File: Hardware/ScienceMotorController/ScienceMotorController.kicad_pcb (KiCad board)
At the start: 2 copper layers, 125.7 x 166.4 mm, 148 parts, among them U1 VNH5019A_E, U10 PMN280ENEAX, U11 PMN280ENEAX, U12 LT1910, U13 LT1910, U14 LT1910, U15 5VA OKI, U2 VNH5019A_E, U3 VNH5019A_E, U4 VNH5019A_E, U5 5V OKI, U6 TM4C129E_Launchpad, U7 3V3 OKI, U8 5VA OKI, U9 PMN280ENEAX

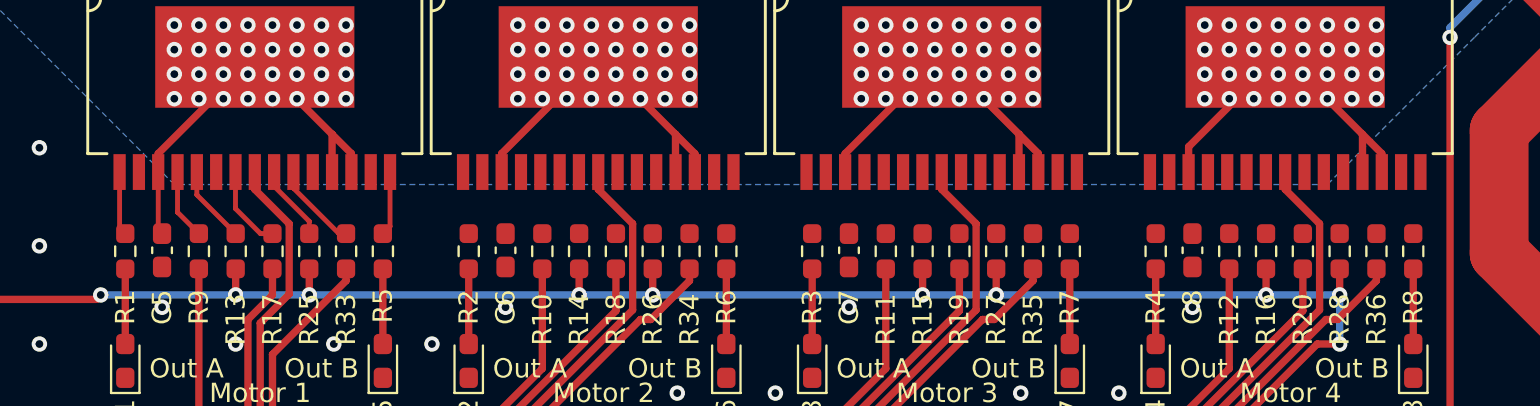
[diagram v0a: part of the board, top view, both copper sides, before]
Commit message: Traces Under Mocos
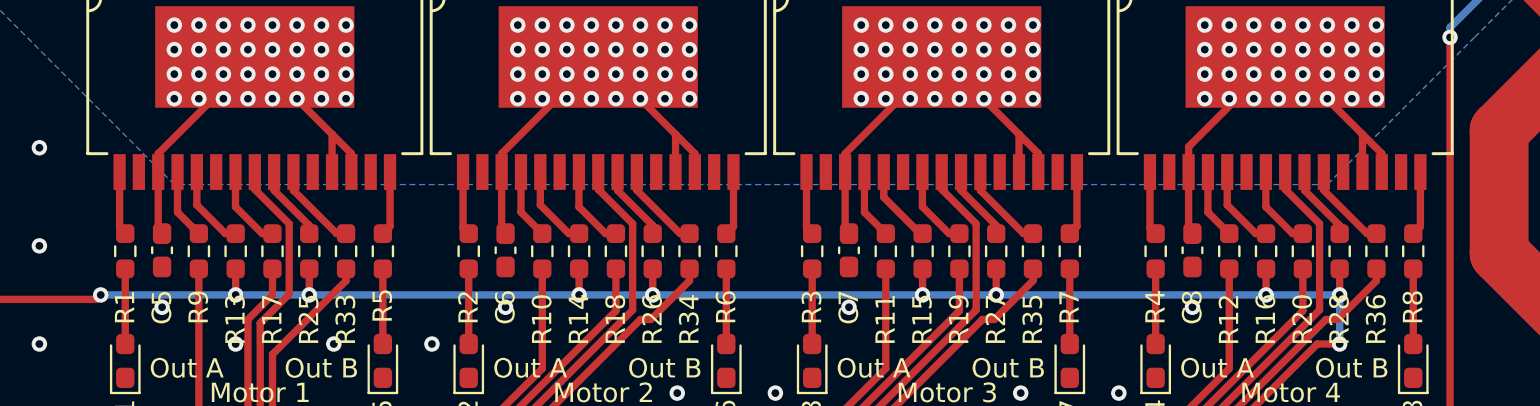
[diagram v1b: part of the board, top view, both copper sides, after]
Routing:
- net +12VA: track 263.1 -> 272.9 mm
- net Net-(R36-Pad1): track 0.00 -> 4.60 mm
- net Net-(R35-Pad1): track 0.00 -> 4.60 mm
- net Net-(R34-Pad1): track 0.00 -> 4.60 mm
- net Net-(R14-Pad1): track 0.00 -> 4.33 mm
- net Net-(R16-Pad1): track 0.00 -> 4.33 mm
- net Net-(R18-Pad1): track 0.00 -> 4.29 mm
- net Net-(R20-Pad1): track 0.00 -> 4.29 mm
- net Net-(R19-Pad1): track 0.00 -> 4.29 mm
- net Net-(R15-Pad1): track 0.00 -> 4.10 mm
- net Net-(R28-Pad1): track 0.00 -> 3.94 mm
- net Net-(R27-Pad1): track 0.00 -> 3.94 mm
- net Net-(R26-Pad1): track 0.00 -> 3.94 mm
- net Net-(R12-Pad1): track 0.00 -> 3.65 mm
- net Net-(R11-Pad1): track 0.00 -> 3.65 mm
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
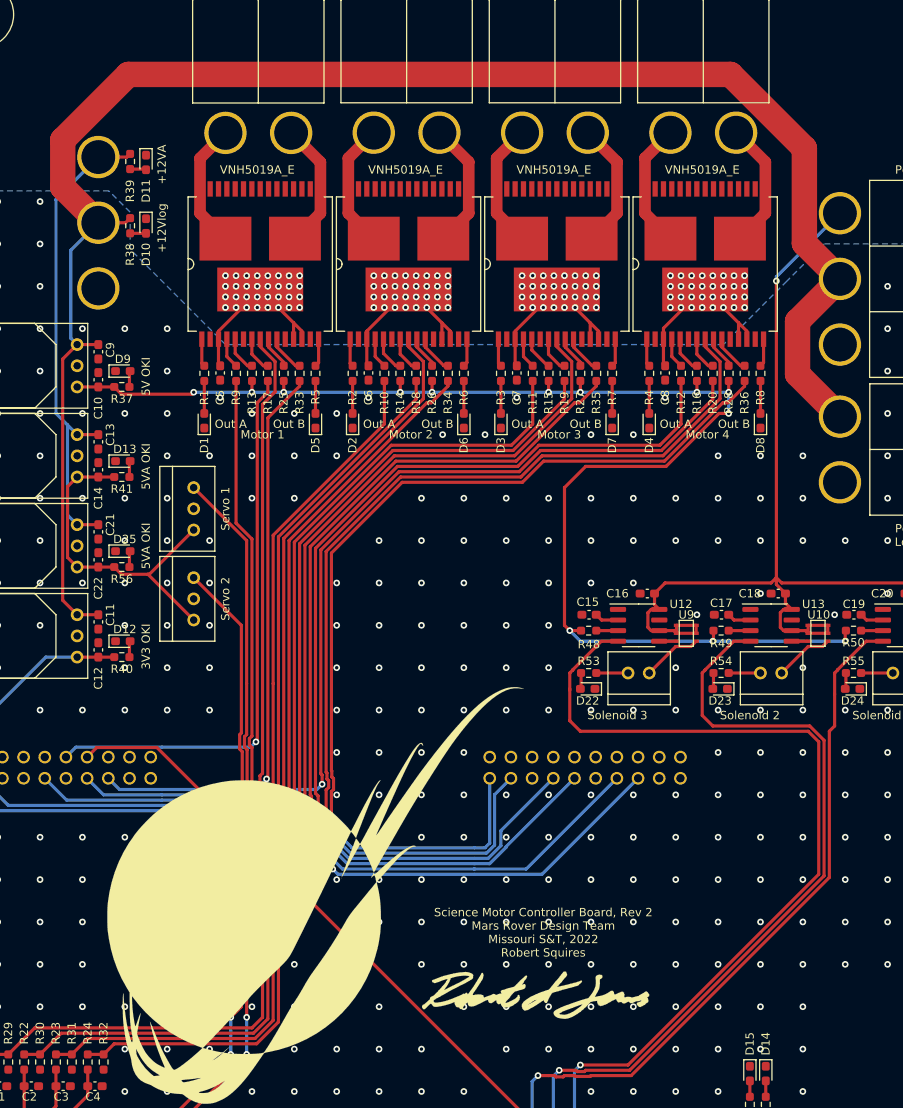
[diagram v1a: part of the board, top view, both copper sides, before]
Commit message: Changed Ground Plane for Motor Stalls
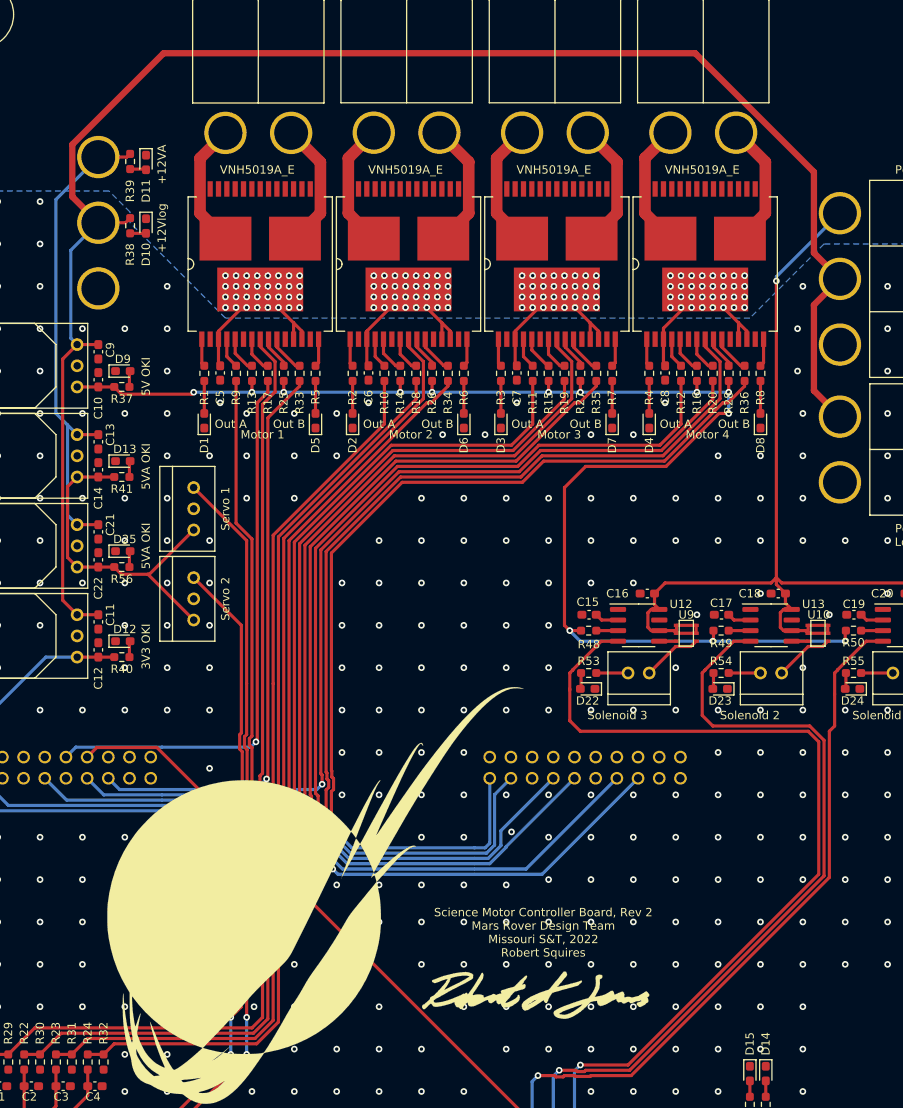
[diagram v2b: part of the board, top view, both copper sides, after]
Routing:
- net +12V: track 204.9 -> 202.4 mm
- net GND: vias 432 -> 438

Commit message: Board Review Changes
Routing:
- net GND: vias 438 -> 421
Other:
- outline, holes or cut-outs redrawn
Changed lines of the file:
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@@
   (general
     (thickness 1.6)
-    (drawings 47)
-    (tracks 1377)
+    (drawings 52)
+    (tracks 1361)
     (zones 0)
     (modules 148)
@@
     )
   )
+  (gr_line (start 141.605 101.6) (end 158.115 101.6) (layer Edge.Cuts) (width 0.05))
+  (gr_line (start 141.605 80.645) (end 141.605 101.6) (layer Edge.Cuts) (width 0.05))
+  (gr_line (start 158.115 80.645) (end 141.605 80.645) (layer Edge.Cuts) (width 0.05))
+  (gr_line (start 160.02 78.105) (end 160.02 78.74) (layer Edge.Cuts) (width 0.05))
+  (gr_arc (start 158.115 78.74) (end 158.115 80.645) (angle -90) (layer Edge.Cuts) (width 0.05))
+  (gr_arc (start 158.115 103.505) (end 160.02 103.505) (angle -90) (layer Edge.Cuts) (width 0.05))
+  (gr_arc (start 156.21 -35.56) (end 160.02 -35.56) (angle -90) (layer Edge.Cuts) (width 0.05))
+  (gr_line (start 160.02 78.105) (end 160.02 -35.56) (layer Edge.Cuts) (width 0.05))
+  (gr_line (start 160.02 123.19) (end 160.02 103.505) (layer Edge.Cuts) (width 0.05))
   (gr_text "Science Motor Controller Board, Rev 2\nMars Rover Design Team\nMissouri S&T, 2022\nRobert Squires" (at 106.045 74.93) (layer F.SilkS)
     (effects (font (size 1 1) (thickness 0.15)))
@@
   )
   (gr_line (start 156.21 127) (end 38.1 127) (layer Edge.Cuts) (width 0.05))
-  (gr_line (start 160.02 113.665) (end 160.02 123.19) (layer Edge.Cuts) (width 0.05))
-  (gr_line (start 160.02 -35.56) (end 160.02 -31.115) (layer Edge.Cuts) (width 0.05))
   (gr_line (start 38.1 -39.37) (end 156.21 -39.37) (layer Edge.Cuts) (width 0.05))
   (gr_line (start 34.29 -35.56) (end 34.29 -31.115) (layer Edge.Cuts) (width 0.05))
   (gr_arc (start 38.1 -35.56) (end 38.1 -39.37) (angle -90) (layer Edge.Cuts) (width 0.05))
-  (gr_arc (start 156.21 -35.56) (end 160.02 -35.56) (angle -90) (layer Edge.Cuts) (width 0.05))
   (gr_arc (start 156.21 123.19) (end 156.21 127) (angle -90) (layer Edge.Cuts) (width 0.05))
   (gr_arc (start 38.1 123.19) (end 34.29 123.19) (angle -90) (layer Edge.Cuts) (width 0.05))
   (gr_line (start 34.29 118.11) (end 34.29 123.19) (layer Edge.Cuts) (width 0.05))
-  (gr_line (start 160.02 -31.115) (end 160.02 113.665) (layer Edge.Cuts) (width 0.05))
   (gr_line (start 34.29 -31.115) (end 34.29 118.11) (layer Edge.Cuts) (width 0.05))
   (segment (start 55.054501 98.226501) (end 53.904 97.076) (width 0.381) (layer F.Cu) (net 1))
@@
   (via (at 147.32 -2.54) (size 0.8) (drill 0.4) (layers F.Cu B.Cu) (net 2))
   (via (at 152.4 -2.54) (size 0.8) (drill 0.4) (layers F.Cu B.Cu) (net 2))
-  (via (at 157.48 -2.54) (size 0.8) (drill 0.4) (layers F.Cu B.Cu) (net 2))
-  (via (at 157.48 2.54) (size 0.8) (drill 0.4) (layers F.Cu B.Cu) (net 2))
   (via (at 152.4 2.54) (size 0.8) (drill 0.4) (layers F.Cu B.Cu) (net 2))
   (via (at 152.4 7.62) (size 0.8) (drill 0.4) (layers F.Cu B.Cu) (net 2))
-  (via (at 157.48 7.62) (size 0.8) (drill 0.4) (layers F.Cu B.Cu) (net 2))
-  (via (at 157.48 12.7) (size 0.8) (drill 0.4) (layers F.Cu B.Cu) (net 2))
   (via (at 152.4 12.7) (size 0.8) (drill 0.4) (layers F.Cu B.Cu) (net 2))
   (via (at 152.4 17.78) (size 0.8) (drill 0.4) (layers F.Cu B.Cu) (net 2))
-  (via (at 157.48 17.78) (size 0.8) (drill 0.4) (layers F.Cu B.Cu) (net 2))
-  (via (at 157.48 22.86) (size 0.8) (drill 0.4) (layers F.Cu B.Cu) (net 2))
   (via (at 152.4 22.86) (size 0.8) (drill 0.4) (layers F.Cu B.Cu) (net 2))
   (via (at 152.4 27.94) (size 0.8) (drill 0.4) (layers F.Cu B.Cu) (net 2))
-  (via (at 157.48 27.94) (size 0.8) (drill 0.4) (layers F.Cu B.Cu) (net 2))
-  (via (at 157.48 33.02) (size 0.8) (drill 0.4) (layers F.Cu B.Cu) (net 2))
   (via (at 152.4 33.02) (size 0.8) (drill 0.4) (layers F.Cu B.Cu) (net 2))
-  (via (at 157.48 38.1) (size 0.8) (drill 0.4) (layers F.Cu B.Cu) (net 2))
-  (via (at 157.48 43.18) (size 0.8) (drill 0.4) (layers F.Cu B.Cu) (net 2))
-  (via (at 157.48 48.26) (size 0.8) (drill 0.4) (layers F.Cu B.Cu) (net 2))
   (via (at 152.4 48.26) (size 0.8) (drill 0.4) (layers F.Cu B.Cu) (net 2))
   (via (at 147.32 48.26) (size 0.8) (drill 0.4) (layers F.Cu B.Cu) (net 2))
@@
   (via (at 152.4 63.5) (size 0.8) (drill 0.4) (layers F.Cu B.Cu) (net 2))
   (via (at 152.4 58.42) (size 0.8) (drill 0.4) (layers F.Cu B.Cu) (net 2))
-  (via (at 157.48 58.42) (size 0.8) (drill 0.4) (layers F.Cu B.Cu) (net 2))
-  (via (at 157.48 63.5) (size 0.8) (drill 0.4) (layers F.Cu B.Cu) (net 2))
-  (via (at 157.48 53.34) (size 0.8) (drill 0.4) (layers F.Cu B.Cu) (net 2))
   (via (at 152.4 53.34) (size 0.8) (drill 0.4) (layers F.Cu B.Cu) (net 2))
   (via (at 147.32 53.34) (size 0.8) (drill 0.4) (layers F.Cu B.Cu) (net 2))
@@
   (via (at 147.32 68.58) (size 0.8) (drill 0.4) (layers F.Cu B.Cu) (net 2))
   (via (at 152.4 68.58) (size 0.8) (drill 0.4) (layers F.Cu B.Cu) (net 2))
-  (via (at 157.48 68.58) (size 0.8) (drill 0.4) (layers F.Cu B.Cu) (net 2))
-  (via (at 157.48 73.66) (size 0.8) (drill 0.4) (layers F.Cu B.Cu) (net 2))
   (via (at 152.4 73.66) (size 0.8) (drill 0.4) (layers F.Cu B.Cu) (net 2))
   (via (at 147.32 73.66) (size 0.8) (drill 0.4) (layers F.Cu B.Cu) (net 2))
@@
   (via (at 147.32 78.74) (size 0.8) (drill 0.4) (layers F.Cu B.Cu) (net 2))
   (via (at 152.4 78.74) (size 0.8) (drill 0.4) (layers F.Cu B.Cu) (net 2))
-  (via (at 157.48 78.74) (size 0.8) (drill 0.4) (layers F.Cu B.Cu) (net 2))
   (via (at 137.16 83.82) (size 0.8) (drill 0.4) (layers F.Cu B.Cu) (net 2))
   (via (at 132.08 83.82) (size 0.8) (drill 0.4) (layers F.Cu B.Cu) (net 2))
@@
   (via (at 147.32 109.22) (size 0.8) (drill 0.4) (layers F.Cu B.Cu) (net 2))
   (via (at 152.4 109.22) (size 0.8) (drill 0.4) (layers F.Cu B.Cu) (net 2))
-  (via (at 157.48 109.22) (size 0.8) (drill 0.4) (layers F.Cu B.Cu) (net 2))
-  (via (at 157.48 104.14) (size 0.8) (drill 0.4) (layers F.Cu B.Cu) (net 2))
   (via (at 152.4 104.14) (size 0.8) (drill 0.4) (layers F.Cu B.Cu) (net 2))
   (via (at 147.32 104.14) (size 0.8) (drill 0.4) (layers F.Cu B.Cu) (net 2))
   (via (at 142.24 104.14) (size 0.8) (drill 0.4) (layers F.Cu B.Cu) (net 2))
-  (via (at 157.48 114.3) (size 0.8) (drill 0.4) (layers F.Cu B.Cu) (net 2))
   (via (at 152.4 114.3) (size 0.8) (drill 0.4) (layers F.Cu B.Cu) (net 2))
   (via (at 147.32 119.38) (size 0.8) (drill 0.4) (layers F.Cu B.Cu) (net 2))
@@
   (via (at 137.16 -2.54) (size 0.8) (drill 0.4) (layers F.Cu B.Cu) (net 2))
   (via (at 66.04 55.245) (size 0.8) (drill 0.4) (layers F.Cu B.Cu) (net 2))
+  (via (at 41.91 95.25) (size 0.8) (drill 0.4) (layers F.Cu B.Cu) (net 2))
+  (via (at 45.72 95.25) (size 0.8) (drill 0.4) (layers F.Cu B.Cu) (net 2))
+  (via (at 48.895 95.25) (size 0.8) (drill 0.4) (layers F.Cu B.Cu) (net 2))
   (segment (start 36.124 111.689) (end 38.1 113.665) (width 0.381) (layer F.Cu) (net 3))
   (segment (start 36.124 99.616) (end 36.124 111.689) (width 0.381) (layer F.Cu) (net 3))
@@
   (segment (start 153.67 38.105) (end 153.67 39.055) (width 0.381) (layer F.Cu) (net 13))
   (segment (start 49.012499 14.087499) (end 47.625 12.7) (width 0.381) (layer B.Cu) (net 13))
-  (via (at 133.985 -3.175) (size 0.8) (drill 0.4) (layers F.Cu B.Cu) (net 13))
-  (segment (start 133.985 -3.683) (end 133.985 -3.175) (width 0.381) (layer B.Cu) (net 13))
-  (segment (start 141.605 -11.303) (end 133.985 -3.683) (width 0.381) (layer B.Cu) (net 13))
   (segment (start 133.985 33.2) (end 135.075 34.29) (width 0.381) (layer F.Cu) (net 13))
   (segment (start 133.35 33.02) (end 133.985 32.385) (width 0.381) (layer F.Cu) (net 13))
@@
   (segment (start 119.38 34.29) (end 120.65 33.02) (width 0.381) (layer F.Cu) (net 13))
   (segment (start 133.985 32.385) (end 133.985 33.2) (width 0.381) (layer F.Cu) (net 13))
-  (segment (start 133.985 -3.175) (end 133.985 32.385) (width 0.381) (layer F.Cu) (net 13))
   (segment (start 151.13 34.29) (end 149.86 33.02) (width 0.381) (layer F.Cu) (net 13))
   (segment (start 149.86 33.02) (end 134.62 33.02) (width 0.381) (layer F.Cu) (net 13))
@@
   (segment (start 120.4506 6.7856) (end 120.65 6.985) (width 0.381) (layer F.Cu) (net 13))
   (segment (start 120.4506 3.7973) (end 120.4506 6.7856) (width 0.381) (layer F.Cu) (net 13))
+  (segment (start 134.62 -4.318) (end 134.62 -3.81) (width 0.762) (layer B.Cu) (net 13))
+  (via (at 134.62 -3.81) (size 0.8) (drill 0.4) (layers F.Cu B.Cu) (net 13))
+  (segment (start 141.605 -11.303) (end 134.62 -4.318) (width 0.762) (layer B.Cu) (net 13))
+  (segment (start 134.62 31.75) (end 133.985 32.385) (width 0.762) (layer F.Cu) (net 13))
+  (segment (start 134.62 -3.81) (end 134.62 31.75) (width 0.762) (layer F.Cu) (net 13))
   (segment (start 48.43149 6.17851) (end 50.165 4.445) (width 0.381) (layer F.Cu) (net 14))
   (segment (start 48.43149 35.09649) (end 48.43149 6.17851) (width 0.381) (layer F.Cu) (net 14))
